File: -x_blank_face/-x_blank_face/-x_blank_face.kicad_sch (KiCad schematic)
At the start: 18 parts

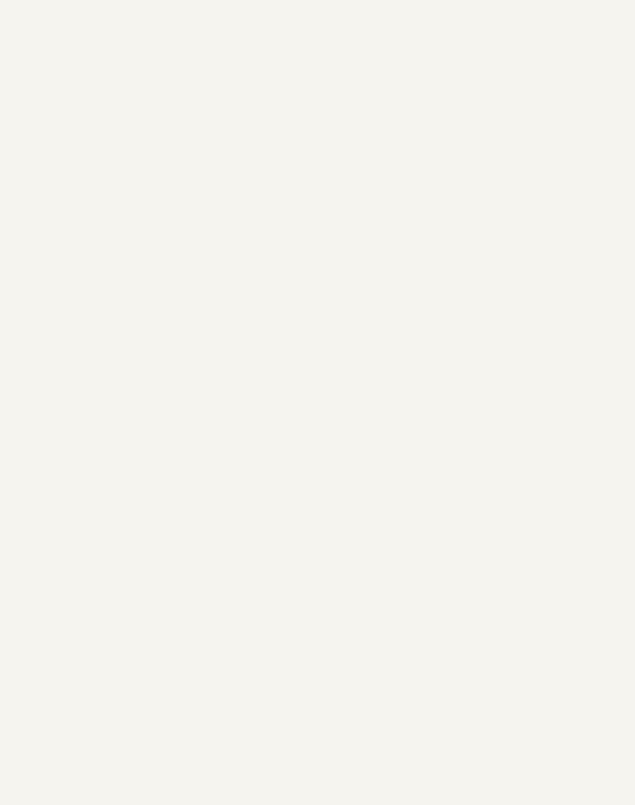
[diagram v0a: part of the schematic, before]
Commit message: Changes solar panels
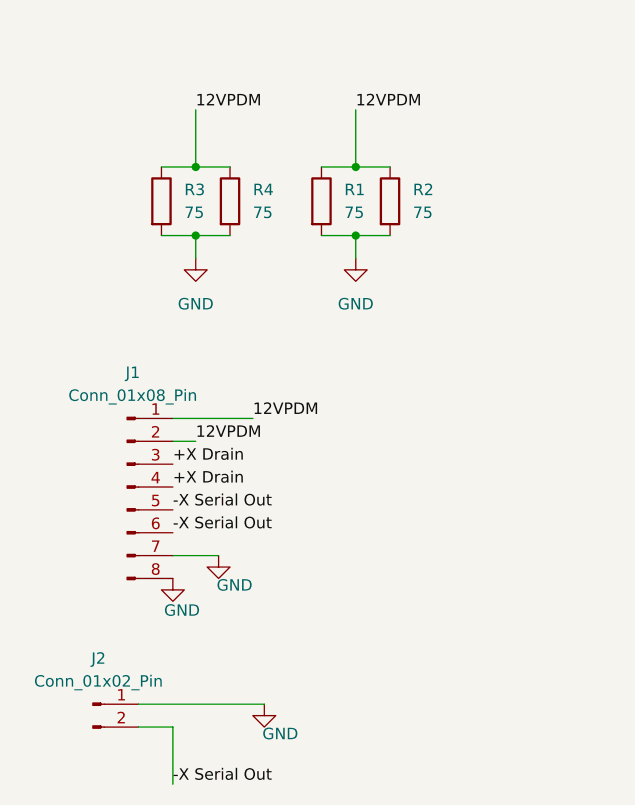
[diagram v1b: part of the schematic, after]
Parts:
- added J1: Conn_01x08_Pin, CNN_GNSS_Footprint:DF13-8P, symbol Connector:Conn_01x08_Pin
- added J2: Conn_01x02_Pin, CNN_GNSS_Footprint:DF13-2P, symbol Connector:Conn_01x02_Pin
- added R1, R2, R3, R4: 75, CNN_GNSS_Footprint:UB3C-75RF1, symbol Device:R
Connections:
- new net +X Drain: J1.3 (Pin_3), J1.4 (Pin_4)
- new net -X Serial Out: J1.5 (Pin_5), J1.6 (Pin_6), J2.2 (Pin_2)
- new net 12VPDM: J1.1 (Pin_1), J1.2 (Pin_2), R1.1, R2.1, R3.1, R4.1
- new net GND: J1.7 (Pin_7), J1.8 (Pin_8), J2.1 (Pin_1), R1.2, R2.2, R3.2, R4.2

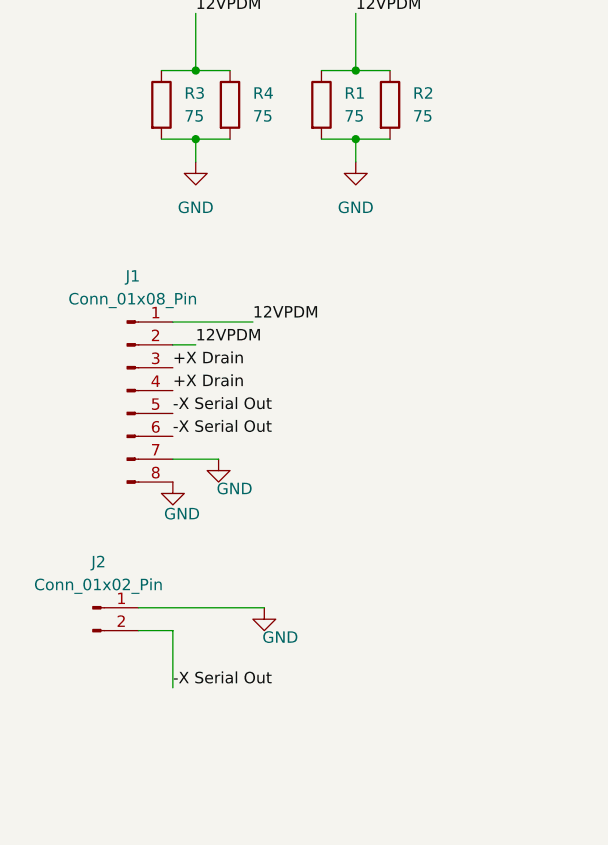
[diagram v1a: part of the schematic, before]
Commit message: added schematic to +x and routed ish the schematic
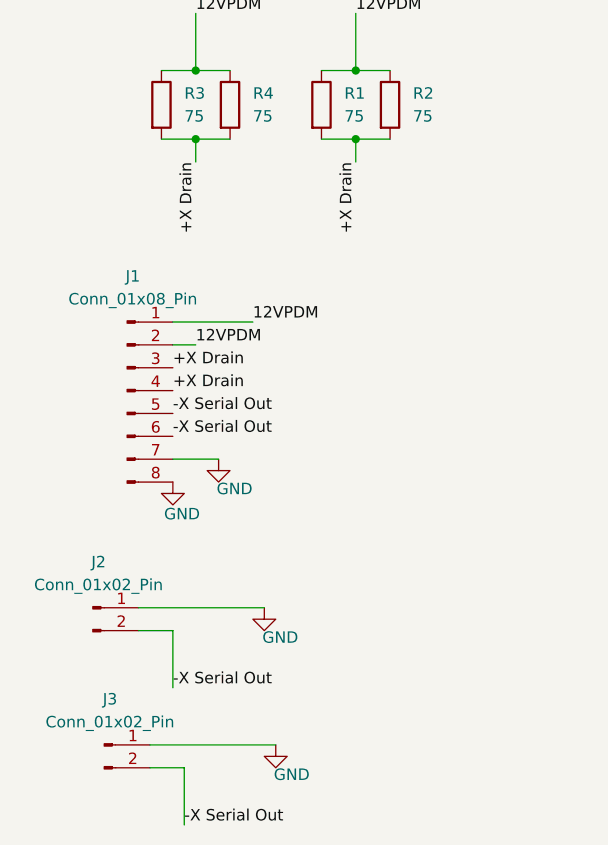
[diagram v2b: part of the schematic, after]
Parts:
- added J3: Conn_01x02_Pin, CNN_GNSS_Footprint:DF13-2P, symbol Connector:Conn_01x02_Pin
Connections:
- net +X Drain: now also R1.2, R2.2, R3.2, R4.2
- net -X Serial Out: now also J3.2 (Pin_2)
- net GND: now also J3.1 (Pin_1); no longer R1.2, R2.2, R3.2, R4.2
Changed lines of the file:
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@@
+	(wire
+		(pts
+			(xy 30.48 139.7) (xy 44.45 139.7)
+		)
+		(stroke
+			(width 0)
+			(type default)
+		)
+	)
 	(wire
 		(pts
@@
 	(wire
 		(pts
-			(xy 38.1 107.95) (xy 33.02 107.95)
+			(xy 34.29 142.24) (xy 30.48 142.24)
 		)
 		(stroke
@@
 	(wire
 		(pts
-			(xy 35.56 74.93) (xy 35.56 72.39)
+			(xy 38.1 107.95) (xy 33.02 107.95)
 		)
 		(stroke
@@
 	(wire
 		(pts
-			(xy 31.75 72.39) (xy 35.56 72.39)
+			(xy 35.56 74.93) (xy 35.56 72.39)
 		)
 		(stroke
@@
 	(wire
 		(pts
-			(xy 53.34 74.93) (xy 53.34 72.39)
+			(xy 31.75 72.39) (xy 35.56 72.39)
 		)
 		(stroke
@@
 	(wire
 		(pts
-			(xy 53.34 64.77) (xy 57.15 64.77)
+			(xy 53.34 74.93) (xy 53.34 72.39)
 		)
 		(stroke
@@
 	(wire
 		(pts
-			(xy 35.56 64.77) (xy 39.37 64.77)
+			(xy 53.34 64.77) (xy 57.15 64.77)
 		)
 		(stroke
@@
 	(wire
 		(pts
+			(xy 35.56 64.77) (xy 39.37 64.77)
+		)
+		(stroke
+			(width 0)
+			(type default)
+		)
+	)
+	(wire
+		(pts
 			(xy 35.56 72.39) (xy 39.37 72.39)
+		)
+		(stroke
+			(width 0)
+			(type default)
+		)
+	)
+	(wire
+		(pts
+			(xy 34.29 148.59) (xy 34.29 142.24)
 		)
 		(stroke
@@
 		)
 	)
+	(label "-X Serial Out"
+		(at 34.29 148.59 0)
+		(effects
+			(font
+				(size 1.27 1.27)
+			)
+			(justify left bottom)
+		)
+	)
 	(label "12VPDM"
 		(at 35.56 95.25 0)
@@
 		)
 	)
+	(label "+X Drain"
+		(at 53.34 74.93 270)
+		(effects
+			(font
+				(size 1.27 1.27)
+			)
+			(justify right bottom)
+		)
+	)
+	(label "+X Drain"
+		(at 35.56 74.93 270)
+		(effects
+			(font
+				(size 1.27 1.27)
+			)
+			(justify right bottom)
+		)
+	)
 	(symbol
 		(lib_id "Mechanical:MountingHole")
@@
 	)
 	(symbol
-		(lib_id "power:GND")
-		(at 53.34 74.93 0)
-		(unit 1)
-		(exclude_from_sim no)
-		(in_bom yes)
-		(on_board yes)
-		(dnp no)
-		(fields_autoplaced yes)
-		(property "Reference" "#PWR01"
-			(at 53.34 81.28 0)
-			(effects
-				(font
-					(size 1.27 1.27)
-				)
-				(hide yes)
-			)
-		)
-		(property "Value" "GND"
-			(at 53.34 80.01 0)
-			(effects
-				(font
-					(size 1.27 1.27)
-				)
-			)
-		)
-		(property "Footprint" ""
-			(at 53.34 74.93 0)
-			(effects
-				(font
-					(size 1.27 1.27)
-				)
-				(hide yes)
-			)
-		)
-		(property "Datasheet" ""
-			(at 53.34 74.93 0)
-			(effects
-				(font
-					(size 1.27 1.27)
-				)
-				(hide yes)
-			)
-		)
-		(property "Description" "Power symbol creates a global label with name \"GND\" , ground"
-			(at 53.34 74.93 0)
-			(effects
-				(font
-					(size 1.27 1.27)
-				)
-				(hide yes)
-			)
-		)
-		(pin "1"
-		)
-		(instances
-			(project ""
-				(path "/ba48ae00-8534-40f4-887e-27846777c670"
-					(reference "#PWR01")
-					(unit 1)
-				)
-			)
-		)
-	)
-	(symbol
 		(lib_id "Mechanical:MountingHole")
 		(at 135.89 50.8 0)
@@
 	)
 	(symbol
+		(lib_id "Connector:Conn_01x02_Pin")
+		(at 25.4 139.7 0)
+		(unit 1)
+		(exclude_from_sim no)
+		(in_bom yes)
+		(on_board yes)
+		(dnp no)
+		(fields_autoplaced yes)
+		(property "Reference" "J3"
+			(at 26.035 134.62 0)
+			(effects
+				(font
+					(size 1.27 1.27)
+				)
+			)
+		)
+		(property "Value" "Conn_01x02_Pin"
+			(at 26.035 137.16 0)
+			(effects
+				(font
+					(size 1.27 1.27)
+				)
+			)
+		)
+		(property "Footprint" "CNN_GNSS_Footprint:DF13-2P"
+			(at 25.4 139.7 0)
+			(effects
+				(font
+					(size 1.27 1.27)
+				)
+				(hide yes)
+			)
+		)
+		(property "Datasheet" "~"
+			(at 25.4 139.7 0)
+			(effects
+				(font
+					(size 1.27 1.27)
+				)
+				(hide yes)
+			)
+		)
+		(property "Description" "Generic connector, single row, 01x02, script generated"
+			(at 25.4 139.7 0)
+			(effects
+				(font
+					(size 1.27 1.27)
+				)
+				(hide yes)
+			)
+		)
+		(pin "1"
+		)
+		(pin "2"
+		)
+		(instances
+			(project "-x_blank_face"
+				(path "/ba48ae00-8534-40f4-887e-27846777c670"
+					(reference "J3")
+					(unit 1)
+				)
+			)
+		)
+	)
+	(symbol
 		(lib_id "Mechanical:MountingHole")
 		(at 165.1 115.57 0)
@@
 	)
 	(symbol
+		(lib_id "power:GND")
+		(at 44.45 139.7 0)
+		(unit 1)
+		(exclude_from_sim no)
+		(in_bom yes)
+		(on_board yes)
+		(dnp no)
+		(property "Reference" "#PWR01"
+			(at 44.45 146.05 0)
+			(effects
+				(font
+					(size 1.27 1.27)
+				)
+				(hide yes)
+			)
+		)
+		(property "Value" "GND"
+			(at 46.228 143.002 0)
+			(effects
+				(font
+					(size 1.27 1.27)
+				)
+			)
+		)
+		(property "Footprint" ""
+			(at 44.45 139.7 0)
+			(effects
+				(font
+					(size 1.27 1.27)
+				)
+				(hide yes)
+			)
+		)
+		(property "Datasheet" ""
+			(at 44.45 139.7 0)
+			(effects
+				(font
+					(size 1.27 1.27)
+				)
+				(hide yes)
+			)
+		)
+		(property "Description" "Power symbol creates a global label with name \"GND\" , ground"
+			(at 44.45 139.7 0)
+			(effects
+				(font
+					(size 1.27 1.27)
+				)
+				(hide yes)
+			)
+		)
+		(pin "1"
+		)
+		(instances
+			(project "-x_blank_face"
+				(path "/ba48ae00-8534-40f4-887e-27846777c670"
+					(reference "#PWR01")
+					(unit 1)
+				)
+			)
+		)
+	)
+	(symbol
 		(lib_id "Mechanical:MountingHole")
 		(at 187.96 114.3 0)
@@
 					(unit 1)
 				)
-			)
-		)
-	)
-	(symbol
-		(lib_id "power:GND")
-		(at 35.56 74.93 0)
-		(unit 1)
-		(exclude_from_sim no)
-		(in_bom yes)
-		(on_board yes)
-		(dnp no)
-		(fields_autoplaced yes)
-		(property "Reference" "#PWR02"
-			(at 35.56 81.28 0)
-			(effects
-				(font
-					(size 1.27 1.27)
-				)
-				(hide yes)
-			)
-		)
-		(property "Value" "GND"
-			(at 35.56 80.01 0)
-			(effects
-				(font
-					(size 1.27 1.27)
-				)
-			)
-		)
-		(property "Footprint" ""
-			(at 35.56 74.93 0)
-			(effects
-				(font
-					(size 1.27 1.27)
-				)
-				(hide yes)
-			)
-		)
-		(property "Datasheet" ""
-			(at 35.56 74.93 0)
-			(effects
-				(font
-					(size 1.27 1.27)
-				)
-				(hide yes)
-			)
-		)
-		(property "Description" "Power symbol creates a global label with name \"GND\" , ground"
-			(at 35.56 74.93 0)
-			(effects
-				(font
-					(size 1.27 1.27)
-				)
-				(hide yes)
-			)
-		)
-		(pin "1"
-		)
-		(instances
-			(project "-x_blank_face"
-				(path "/ba48ae00-8534-40f4-887e-27846777c670"
-					(reference "#PWR02")
-					(unit 1)
-				)

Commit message: changed switch connector footprint
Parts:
- J2, J3: footprint CNN_GNSS_Footprint:DF13-2P -> CNN_GNSS_Footprint:CON2_1X2_UR_DF13
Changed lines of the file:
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@@
 			)
 		)
-		(property "Footprint" "CNN_GNSS_Footprint:DF13-2P"
+		(property "Footprint" "CNN_GNSS_Footprint:CON2_1X2_UR_DF13"
 			(at 25.4 139.7 0)
 			(effects
@@
 			)
 		)
-		(property "Footprint" "CNN_GNSS_Footprint:DF13-2P"
+		(property "Footprint" "CNN_GNSS_Footprint:CON2_1X2_UR_DF13"
 			(at 24.13 124.46 0)
 			(effects
